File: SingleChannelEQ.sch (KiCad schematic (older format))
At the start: 2 parts

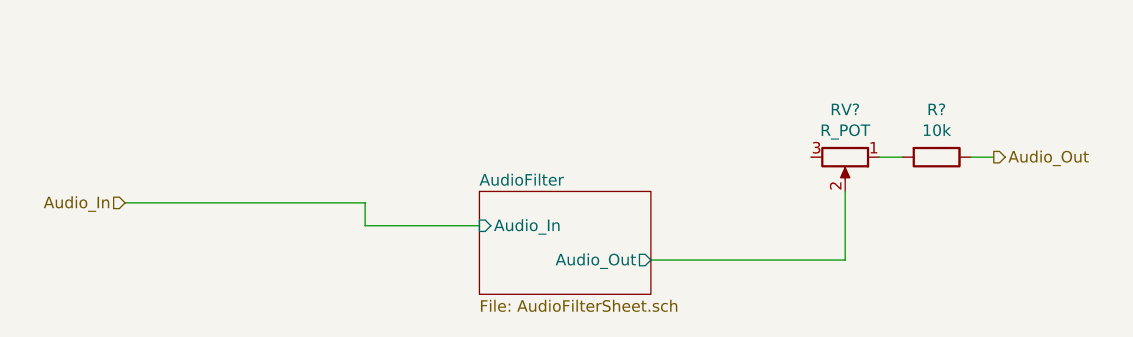
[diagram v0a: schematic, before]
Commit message: Filter calculations, gain stage, oscillation protection
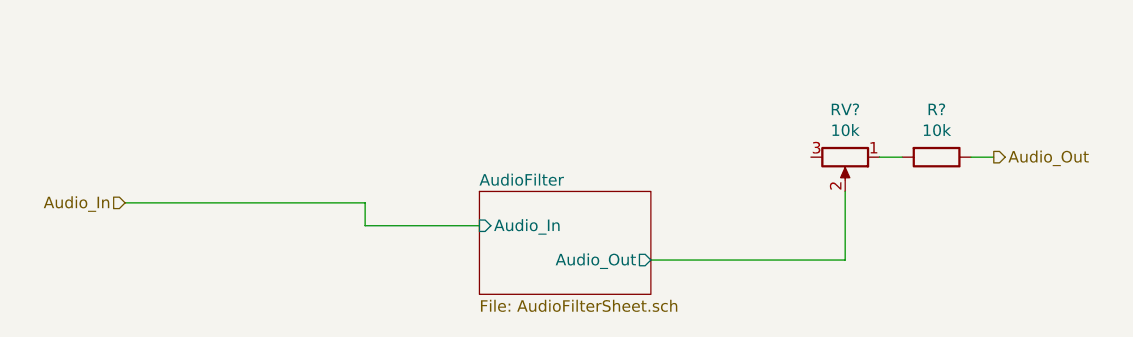
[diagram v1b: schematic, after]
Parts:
- RV?: value R_POT -> 10k
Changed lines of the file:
@@
 AR Path="/5E41292B/5E4118E7" Ref="RV?"  Part="1"
 F 0 "RV?" V 5243 2200 50  0000 C CNN
-F 1 "R_POT" V 5334 2200 50  0000 C CNN
+F 1 "10k" V 5334 2200 50  0000 C CNN
 F 2 "" H 5450 2200 50  0001 C CNN
 F 3 "~" H 5450 2200 50  0001 C CNN

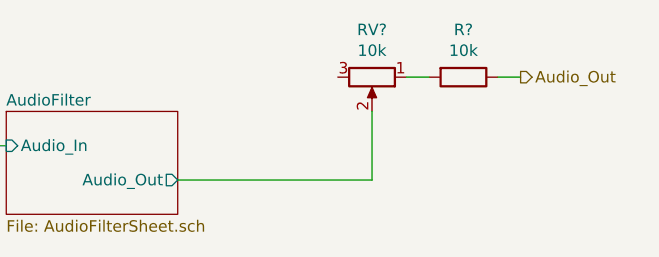
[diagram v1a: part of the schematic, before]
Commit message: Ferrite beads and annotations
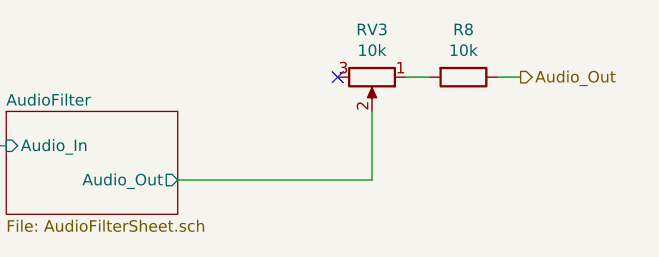
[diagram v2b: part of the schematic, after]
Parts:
- gave numbers to parts that had none: 2
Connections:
- no-connect marks 0 -> 1
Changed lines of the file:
@@
 	3350 2500 3850 2500
 $Comp
-L Device:R_POT RV?
+L Device:R_POT RV1
 U 1 1 5E4118E7
 P 5450 2200
-AR Path="/5E39A5DA/5E4118E7" Ref="RV?"  Part="1"
-AR Path="/5E41281A/5E4118E7" Ref="RV?"  Part="1"
-AR Path="/5E41292B/5E4118E7" Ref="RV?"  Part="1"
-F 0 "RV?" V 5243 2200 50  0000 C CNN
+AR Path="/5E39A5DA/5E4118E7" Ref="RV1"  Part="1"
+AR Path="/5E41281A/5E4118E7" Ref="RV2"  Part="1"
+AR Path="/5E41292B/5E4118E7" Ref="RV3"  Part="1"
+F 0 "RV3" V 5243 2200 50  0000 C CNN
 F 1 "10k" V 5334 2200 50  0000 C CNN
 F 2 "" H 5450 2200 50  0001 C CNN
@@
 	5450 2650 5450 2350
 $Comp
-L Device:R R?
+L Device:R R3
 U 1 1 5E4A2D28
 P 5850 2200
-F 0 "R?" V 5643 2200 50  0000 C CNN
+AR Path="/5E39A5DA/5E4A2D28" Ref="R3"  Part="1"
+AR Path="/5E41281A/5E4A2D28" Ref="R7"  Part="1"
+AR Path="/5E41292B/5E4A2D28" Ref="R8"  Part="1"
+F 0 "R8" V 5643 2200 50  0000 C CNN
 F 1 "10k" V 5734 2200 50  0000 C CNN
 F 2 "" V 5780 2200 50  0001 C CNN
@@
 Wire Wire Line
 	6000 2200 6100 2200
+NoConn ~ 5300 2200
 $EndSCHEMATC

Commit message: Layout, 2020-05 order
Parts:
- R3: footprint (none) -> Resistors_SMD:R_0805_HandSoldering
- RV1: footprint (none) -> BVH_Components_Misc:Potentiometer_TT_P090S-Top-Adjust
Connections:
- net at RV1.1: no longer R3.2
- net at RV1.3: now also R3.2
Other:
- moved on the sheet: R3
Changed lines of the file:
@@
 Text HLabel 2300 2400 0    50   Input ~ 0
 Audio_In
-Text HLabel 6100 2200 2    50   Output ~ 0
+Text HLabel 5700 1850 2    50   Output ~ 0
 Audio_Out
 Wire Wire Line
@@
 AR Path="/5E41281A/5E4118E7" Ref="RV2"  Part="1"
 AR Path="/5E41292B/5E4118E7" Ref="RV3"  Part="1"
-F 0 "RV3" V 5243 2200 50  0000 C CNN
+F 0 "RV1" V 5243 2200 50  0000 C CNN
 F 1 "10k" V 5334 2200 50  0000 C CNN
-F 2 "" H 5450 2200 50  0001 C CNN
+F 2 "BVH_Components_Misc:Potentiometer_TT_P090S-Top-Adjust" H 5450 2200 50  0001 C CNN
 F 3 "~" H 5450 2200 50  0001 C CNN
 	1    5450 2200
@@
 L Device:R R3
 U 1 1 5E4A2D28
-P 5850 2200
+P 5450 1850
 AR Path="/5E39A5DA/5E4A2D28" Ref="R3"  Part="1"
 AR Path="/5E41281A/5E4A2D28" Ref="R7"  Part="1"
 AR Path="/5E41292B/5E4A2D28" Ref="R8"  Part="1"
-F 0 "R8" V 5643 2200 50  0000 C CNN
-F 1 "10k" V 5734 2200 50  0000 C CNN
-F 2 "" V 5780 2200 50  0001 C CNN
-F 3 "~" H 5850 2200 50  0001 C CNN
-	1    5850 2200
+F 0 "R3" V 5243 1850 50  0000 C CNN
+F 1 "10k" V 5334 1850 50  0000 C CNN
+F 2 "Resistors_SMD:R_0805_HandSoldering" V 5380 1850 50  0001 C CNN
+F 3 "~" H 5450 1850 50  0001 C CNN
+	1    5450 1850
 	0    1    1    0
 $EndComp
 Wire Wire Line
-	5700 2200 5600 2200
+	5600 1850 5700 1850
+NoConn ~ 5450 2050
 Wire Wire Line
-	6000 2200 6100 2200
-NoConn ~ 5300 2200
+	5300 2200 5300 1850
 $EndSCHEMATC
